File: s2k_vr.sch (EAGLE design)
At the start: 57 parts, among them IC1 MKE04Z8VWJ4, IC2 MAX9926, IC3 LTC6903, IC4 74LVC2G32DP, Q1 12MHz

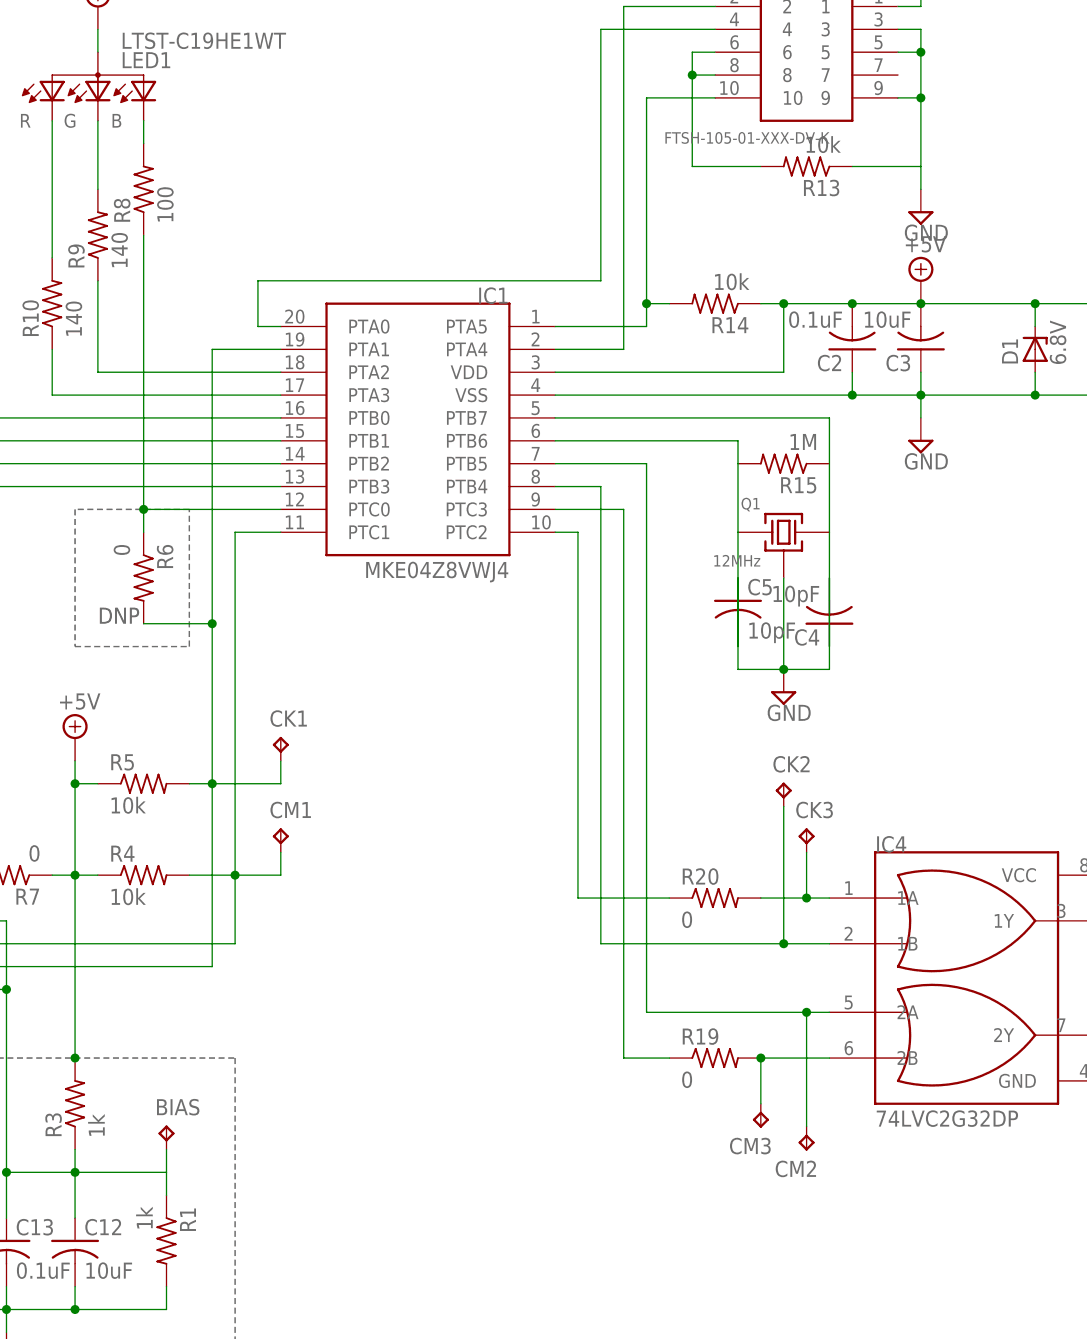
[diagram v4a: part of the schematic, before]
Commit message: Replace crystal with CX2520DB and reshuffle timer output channels.
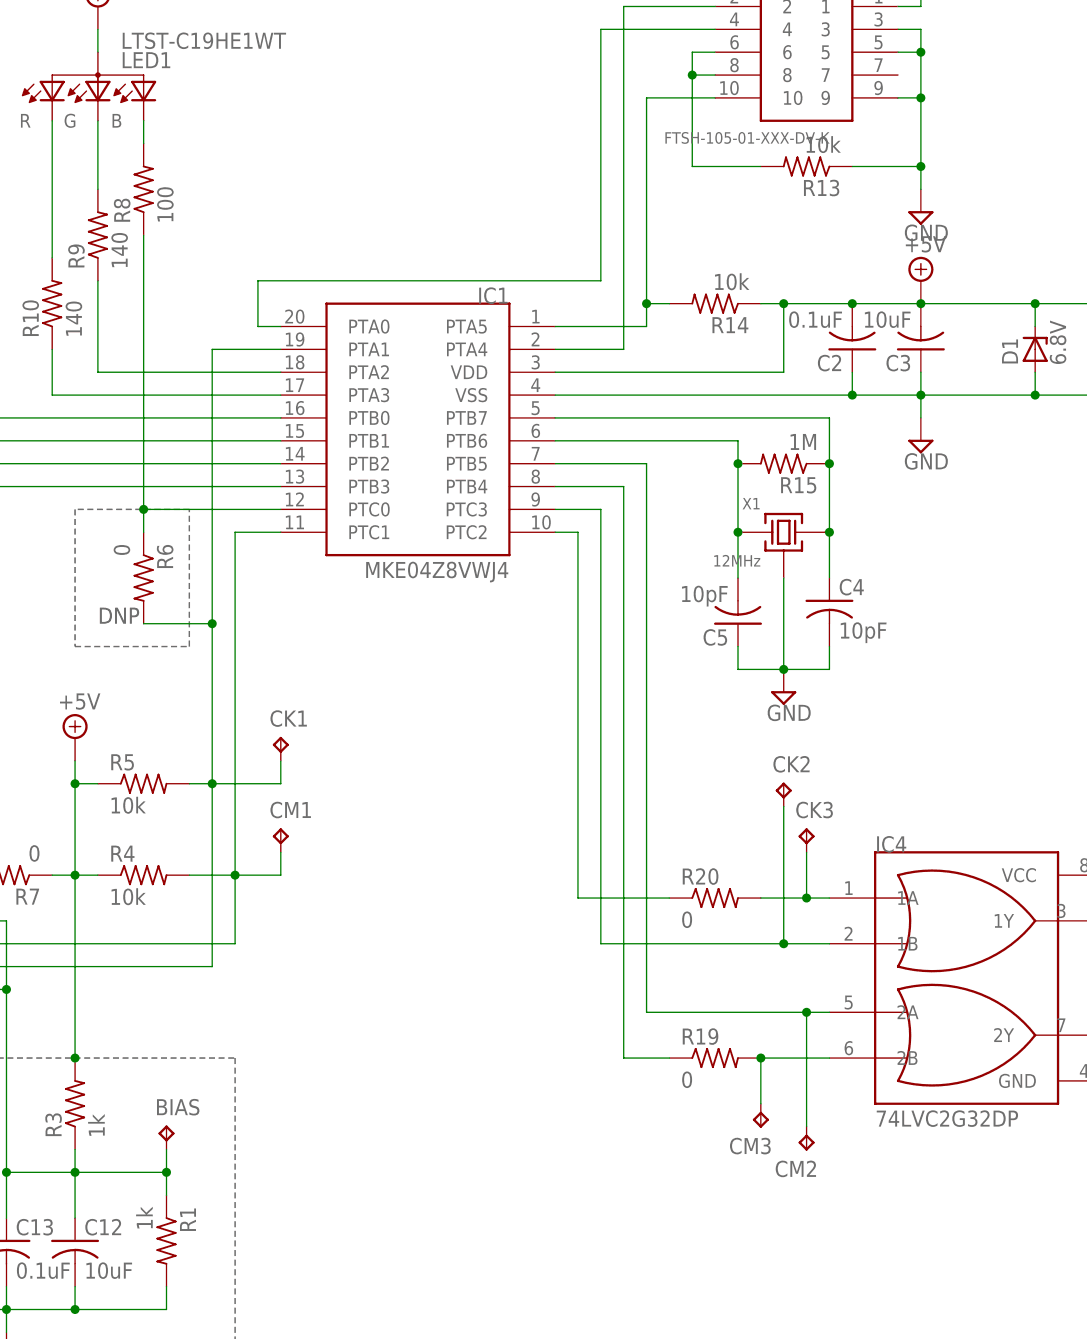
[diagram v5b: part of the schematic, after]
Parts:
- removed Q1: 12MHz, parts:ABM10-167
- added X1: 12MHz, parts:CX2520DB
- C12, C13, R1, R2, R3, R6: DNP (none) -> DNP
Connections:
- net CAM_PULSE: now also IC1.PTC3; no longer IC1.PTB4
- net GND: now also X1.GND; no longer Q1.GND
- net N$10: now also X1.1; no longer Q1.1
- net N$15: now also IC1.PTB4; no longer IC1.PTC3
- net N$26: now also X1.2; no longer Q1.2
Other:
- moved on the sheet: C4, C5
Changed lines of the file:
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@@
 <part name="SUPPLY5" library="supply2" deviceset="+5V" device=""/>
 <part name="R3" library="resistor" deviceset="R-US_" device="R0603" value="1k">
-<attribute name="DNP" value=""/>
+<attribute name="DNP" value="DNP"/>
 </part>
 <part name="R1" library="resistor" deviceset="R-US_" device="R0603" value="1k">
-<attribute name="DNP" value=""/>
+<attribute name="DNP" value="DNP"/>
 </part>
 <part name="R12" library="resistor" deviceset="R-US_" device="R0603" value="10k"/>
@@
 <part name="C9" library="resistor" deviceset="C-US" device="C0805" value="10uF"/>
 <part name="C12" library="resistor" deviceset="C-US" device="C0603" value="10uF">
-<attribute name="DNP" value=""/>
+<attribute name="DNP" value="DNP"/>
 </part>
 <part name="C5" library="resistor" deviceset="C-US" device="C0603" value="10pF"/>
@@
 <part name="SUPPLY12" library="supply2" deviceset="GND" device=""/>
 <part name="C13" library="resistor" deviceset="C-US" device="C0603" value="0.1uF">
-<attribute name="DNP" value=""/>
+<attribute name="DNP" value="DNP"/>
 </part>
 <part name="C8" library="parts" deviceset="CAP-0306" device="" value="10nF"/>
@@
 <part name="SUPPLY16" library="supply2" deviceset="+5V" device=""/>
 <part name="R6" library="resistor" deviceset="R-US_" device="R0603" value="0">
-<attribute name="DNP" value=""/>
+<attribute name="DNP" value="DNP"/>
 </part>
 <part name="CM1" library="testpad" deviceset="TP" device="B2,54"/>
@@
 <part name="D1" library="diode" deviceset="ZENER-DIODE" device="SOT23" value="6.8V"/>
 <part name="SGND" library="wirepad" deviceset="3,81/1,4" device=""/>
-<part name="Q1" library="parts" deviceset="ABM10-167" device="" value="12MHz"/>
+<part name="X1" library="parts" deviceset="CX2520DB" device="" value="12MHz"/>
 <part name="R21" library="resistor" deviceset="R-US_" device="R0603" value="100"/>
 <part name="R22" library="resistor" deviceset="R-US_" device="R0603" value="100"/>
@@
 <part name="SUPPLY6" library="supply2" deviceset="GND" device=""/>
 <part name="R2" library="resistor" deviceset="R-US_" device="R0603" value="0">
-<attribute name="DNP" value=""/>
+<attribute name="DNP" value="DNP"/>
 </part>
 <part name="R11" library="resistor" deviceset="R-US_" device="R0603" value="10k"/>
@@
 <attribute name="DNP" x="-7.62" y="-66.04" size="1.778" layer="96" display="off"/>
 </instance>
-<instance part="C5" gate="G$1" x="66.04" y="5.08"/>
-<instance part="C4" gate="G$1" x="76.2" y="2.54" rot="R180"/>
+<instance part="C5" gate="G$1" x="66.04" y="2.54" rot="R180"/>
+<instance part="C4" gate="G$1" x="76.2" y="5.08"/>
 <instance part="SUPPLY2" gate="GND" x="71.12" y="-5.08"/>
 <instance part="SUPPLY7" gate="+5V" x="86.36" y="40.64"/>
@@
 <instance part="D1" gate="G$1" x="99.06" y="33.02" rot="R90"/>
 <instance part="SGND" gate="1" x="-119.38" y="-15.24"/>
-<instance part="Q1" gate="G$1" x="71.12" y="12.7" rot="MR0"/>
+<instance part="X1" gate="G$1" x="71.12" y="12.7" rot="MR0"/>
 <instance part="R21" gate="G$1" x="114.3" y="-30.48" rot="R180"/>
 <instance part="R22" gate="G$1" x="114.3" y="-43.18" rot="R180"/>
@@
 <net name="CAM_PULSE" class="0">
 <segment>
-<wire x1="50.8" y1="17.78" x2="50.8" y2="-33.02" width="0.1524" layer="91"/>
+<wire x1="50.8" y1="15.24" x2="50.8" y2="-33.02" width="0.1524" layer="91"/>
 <wire x1="50.8" y1="-33.02" x2="71.12" y2="-33.02" width="0.1524" layer="91"/>
 <pinref part="CK2" gate="G$1" pin="TP"/>
 <wire x1="71.12" y1="-17.78" x2="71.12" y2="-33.02" width="0.1524" layer="91"/>
-<pinref part="IC1" gate="G$1" pin="PTB4"/>
-<wire x1="50.8" y1="17.78" x2="45.72" y2="17.78" width="0.1524" layer="91"/>
 <pinref part="IC4" gate="G$1" pin="1B"/>
 <wire x1="71.12" y1="-33.02" x2="76.2" y2="-33.02" width="0.1524" layer="91"/>
 <junction x="71.12" y="-33.02"/>
+<pinref part="IC1" gate="G$1" pin="PTC3"/>
+<wire x1="50.8" y1="15.24" x2="45.72" y2="15.24" width="0.1524" layer="91"/>
 </segment>
 </net>
@@
 <wire x1="66.04" y1="22.86" x2="66.04" y2="20.32" width="0.1524" layer="91"/>
 <pinref part="R15" gate="G$1" pin="2"/>
-<pinref part="Q1" gate="G$1" pin="2"/>
+<pinref part="X1" gate="G$1" pin="2"/>
 <wire x1="66.04" y1="20.32" x2="66.04" y2="12.7" width="0.1524" layer="91"/>
 <pinref part="C5" gate="G$1" pin="2"/>
-<wire x1="66.04" y1="12.7" x2="66.04" y2="0" width="0.1524" layer="91"/>
+<wire x1="66.04" y1="12.7" x2="66.04" y2="7.62" width="0.1524" layer="91"/>
+<junction x="66.04" y="12.7"/>
+<junction x="66.04" y="20.32"/>
 </segment>
 </net>
@@
 <pinref part="R3" gate="G$1" pin="1"/>
 <wire x1="-7.62" y1="-55.88" x2="-7.62" y2="-58.42" width="0.1524" layer="91"/>
+<junction x="2.54" y="-58.42"/>
 </segment>
 </net>
@@
 <net name="N$10" class="0">
 <segment>
-<pinref part="Q1" gate="G$1" pin="1"/>
+<pinref part="X1" gate="G$1" pin="1"/>
 <pinref part="C4" gate="G$1" pin="1"/>
-<wire x1="76.2" y1="12.7" x2="76.2" y2="0" width="0.1524" layer="91"/>
+<wire x1="76.2" y1="12.7" x2="76.2" y2="7.62" width="0.1524" layer="91"/>
 <pinref part="IC1" gate="G$1" pin="PTB7"/>
 <wire x1="45.72" y1="25.4" x2="76.2" y2="25.4" width="0.1524" layer="91"/>
@@
 <pinref part="R15" gate="G$1" pin="1"/>
 <wire x1="76.2" y1="12.7" x2="76.2" y2="20.32" width="0.1524" layer="91"/>
+<junction x="76.2" y="12.7"/>
+<junction x="76.2" y="20.32"/>
 </segment>
 </net>
@@
 <net name="N$15" class="0">
 <segment>
-<pinref part="IC1" gate="G$1" pin="PTC3"/>
-<wire x1="45.72" y1="15.24" x2="53.34" y2="15.24" width="0.1524" layer="91"/>
-<wire x1="53.34" y1="15.24" x2="53.34" y2="-45.72" width="0.1524" layer="91"/>
+<wire x1="53.34" y1="17.78" x2="53.34" y2="-45.72" width="0.1524" layer="91"/>
 <pinref part="R19" gate="G$1" pin="1"/>
 <wire x1="53.34" y1="-45.72" x2="58.42" y2="-45.72" width="0.1524" layer="91"/>
+<pinref part="IC1" gate="G$1" pin="PTB4"/>
+<wire x1="53.34" y1="17.78" x2="45.72" y2="17.78" width="0.1524" layer="91"/>
 </segment>
 </net>
@@
 <pinref part="R13" gate="G$1" pin="1"/>
 <wire x1="78.74" y1="53.34" x2="86.36" y2="53.34" width="0.1524" layer="91"/>
+<junction x="86.36" y="53.34"/>
 </segment>
 <segment>
@@
 <pinref part="SUPPLY2" gate="GND" pin="GND"/>
 <junction x="71.12" y="-2.54"/>
-<pinref part="Q1" gate="G$1" pin="GND"/>
+<pinref part="X1" gate="G$1" pin="GND"/>
 <wire x1="71.12" y1="7.62" x2="71.12" y2="-2.54" width="0.1524" layer="91"/>
 <wire x1="71.12" y1="-2.54" x2="66.04" y2="-2.54" width="0.1524" layer="91"/>
-<wire x1="66.04" y1="-2.54" x2="66.04" y2="7.62" width="0.1524" layer="91"/>
+<wire x1="66.04" y1="-2.54" x2="66.04" y2="0" width="0.1524" layer="91"/>
 <wire x1="71.12" y1="-2.54" x2="76.2" y2="-2.54" width="0.1524" layer="91"/>
-<wire x1="76.2" y1="-2.54" x2="76.2" y2="7.62" width="0.1524" layer="91"/>
-</segment>
-<segment>
+<wire x1="76.2" y1="-2.54" x2="76.2" y2="0" width="0.1524" layer="91"/>
+</segment>
+<segment>
